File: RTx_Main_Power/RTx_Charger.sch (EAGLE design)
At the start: 15 parts, among them IC1 TL331

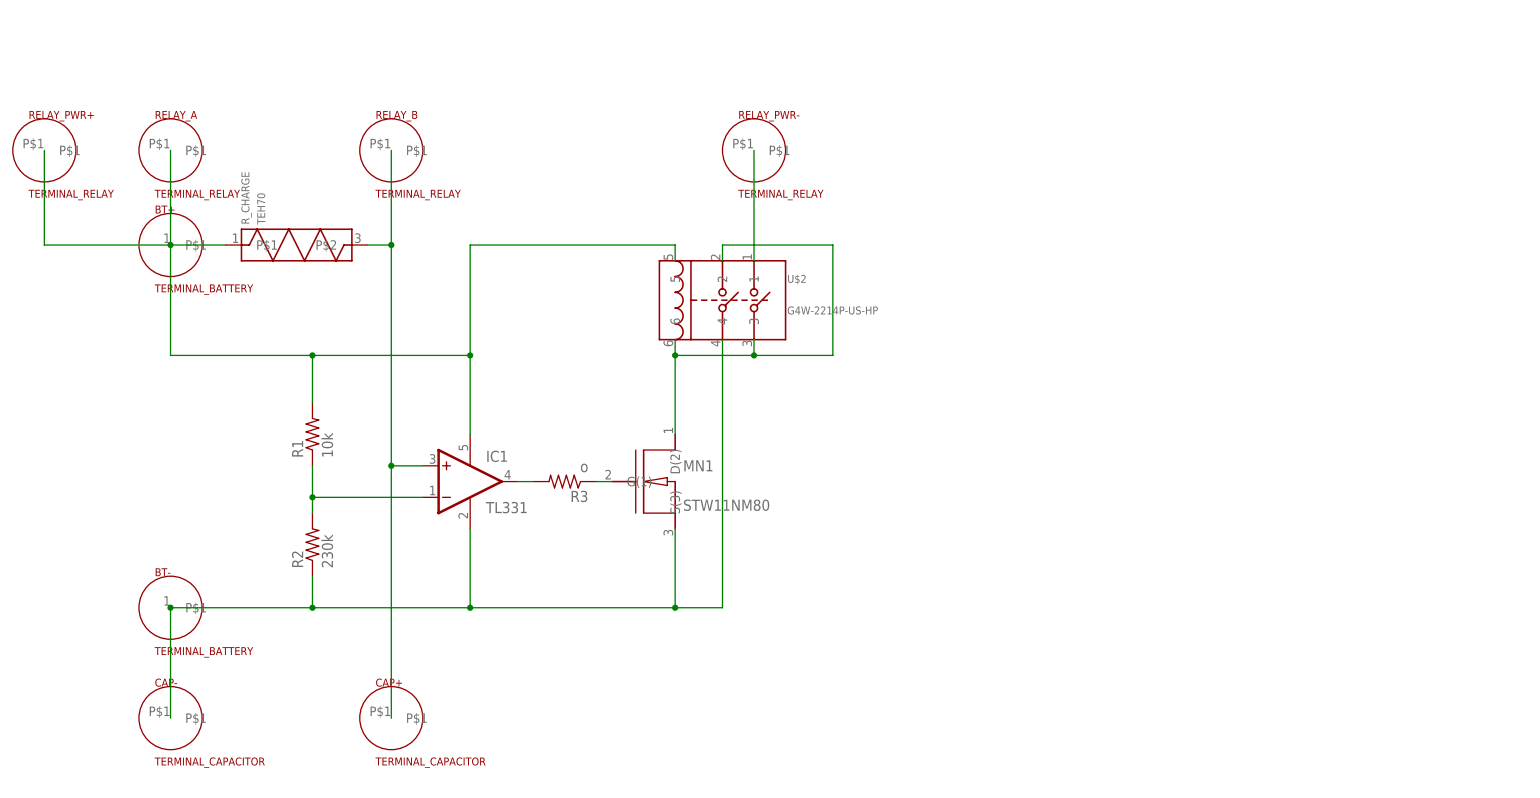
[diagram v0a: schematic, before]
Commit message: Most recent WPR.docx. Updated charger circuit to reflect potential issue fix.
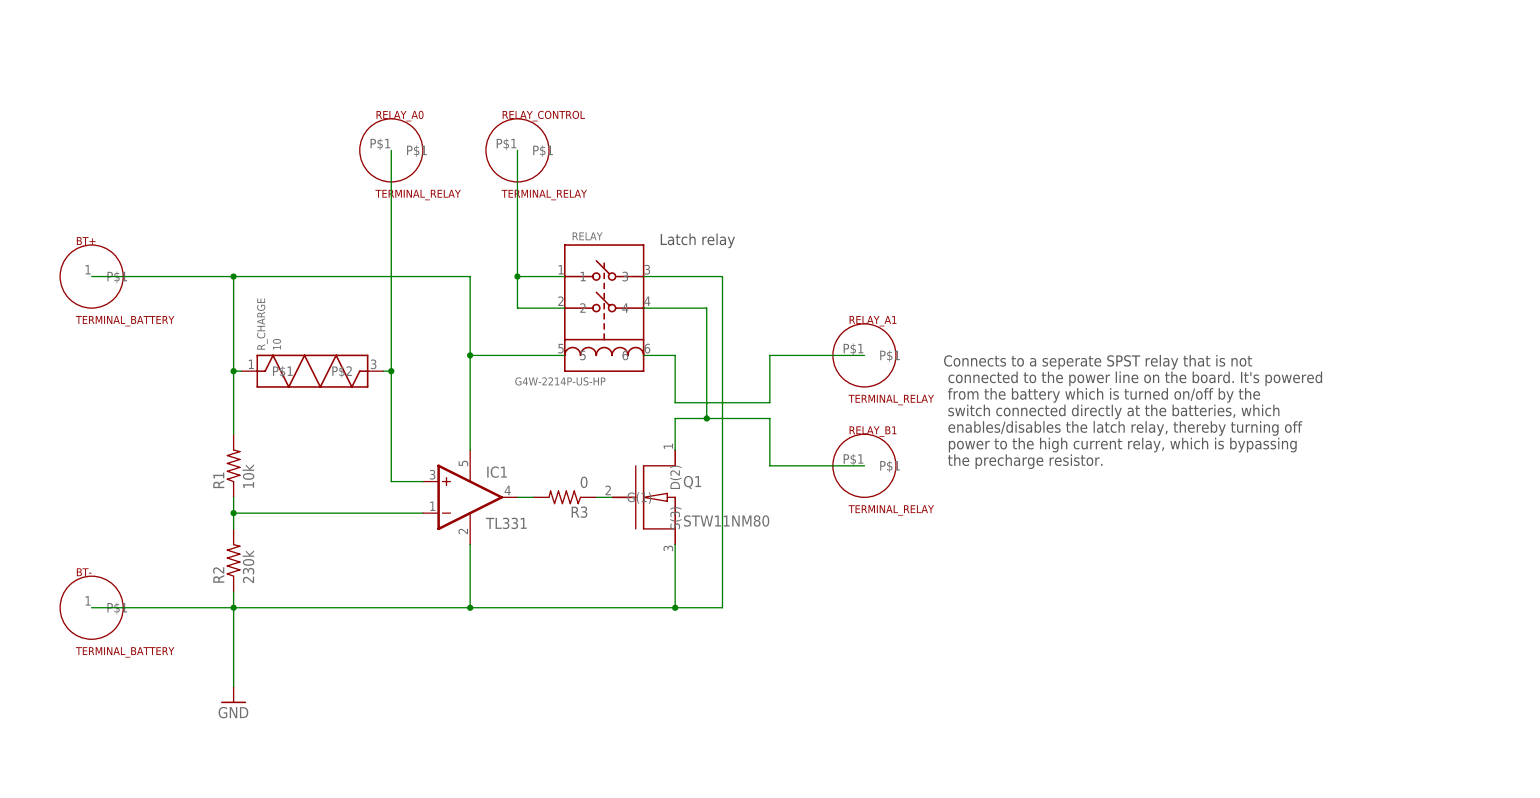
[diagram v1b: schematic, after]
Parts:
- removed CAP+, CAP-: TERMINAL_CAPACITOR, temp_library:TERMINAL_CAPACITOR
- removed MN1: STW11NM80, temp_library:STW11NM80
- removed RELAY_A, RELAY_PWR+, RELAY_PWR-: TERMINAL_RELAY, temp_library:TERMINAL_RELAY
- removed U$2: G4W-2214P-US-HP, temp_library:G4W-2214P-US-HP
- added Q1: STW11NM80, temp_library:STW11NM80
- added RELAY: G4W-2214P-US-HP, temp_library:G4W-2214P-US-HP
- added RELAY_A1, RELAY_B1, RELAY_CONTROL: TERMINAL_RELAY, temp_library:TERMINAL_RELAY
- R3: value o -> 0
- R_CHARGE: value TEH70 -> 10
- renumbered RELAY_B to RELAY_A0
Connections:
- removed net N$2: RELAY_PWR-.P$1, U$2.1
- new net N$7: RELAY.1, RELAY.2, RELAY_CONTROL.P$1
- new net N$8: RELAY.6, RELAY_A1.P$1
- new net N$9: Q1.D(2), RELAY.4, RELAY_B1.P$1
- net GND: now also Q1.S(3), RELAY.3; no longer CAP-.P$1, MN1.S(3), U$2.4
- net N$3: now also BT+.P$1; no longer MN1.D(2), U$2.2, U$2.3, U$2.6
- net N$5: now also Q1.G(1); no longer MN1.G(1)
- net N$6: no longer CAP+.P$1
- net VDD: now also RELAY.5; no longer BT+.P$1, RELAY_A.P$1, RELAY_PWR+.P$1, U$2.5
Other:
- note added: "Connects to a seperate SPST relay that is not connected to the power line on the board. It's powered from the battery which is turned on/off by the switch connected directly at the batteries, which enables/disables the latch relay, thereby turning off power to the high current relay, which is bypassing the precharge resistor."
- note added: "Latch relay"
- moved on the sheet: BT+, BT-, IC1, R1, R2, R3, R_CHARGE

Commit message: Added additional terminals to RTx_Charger board.
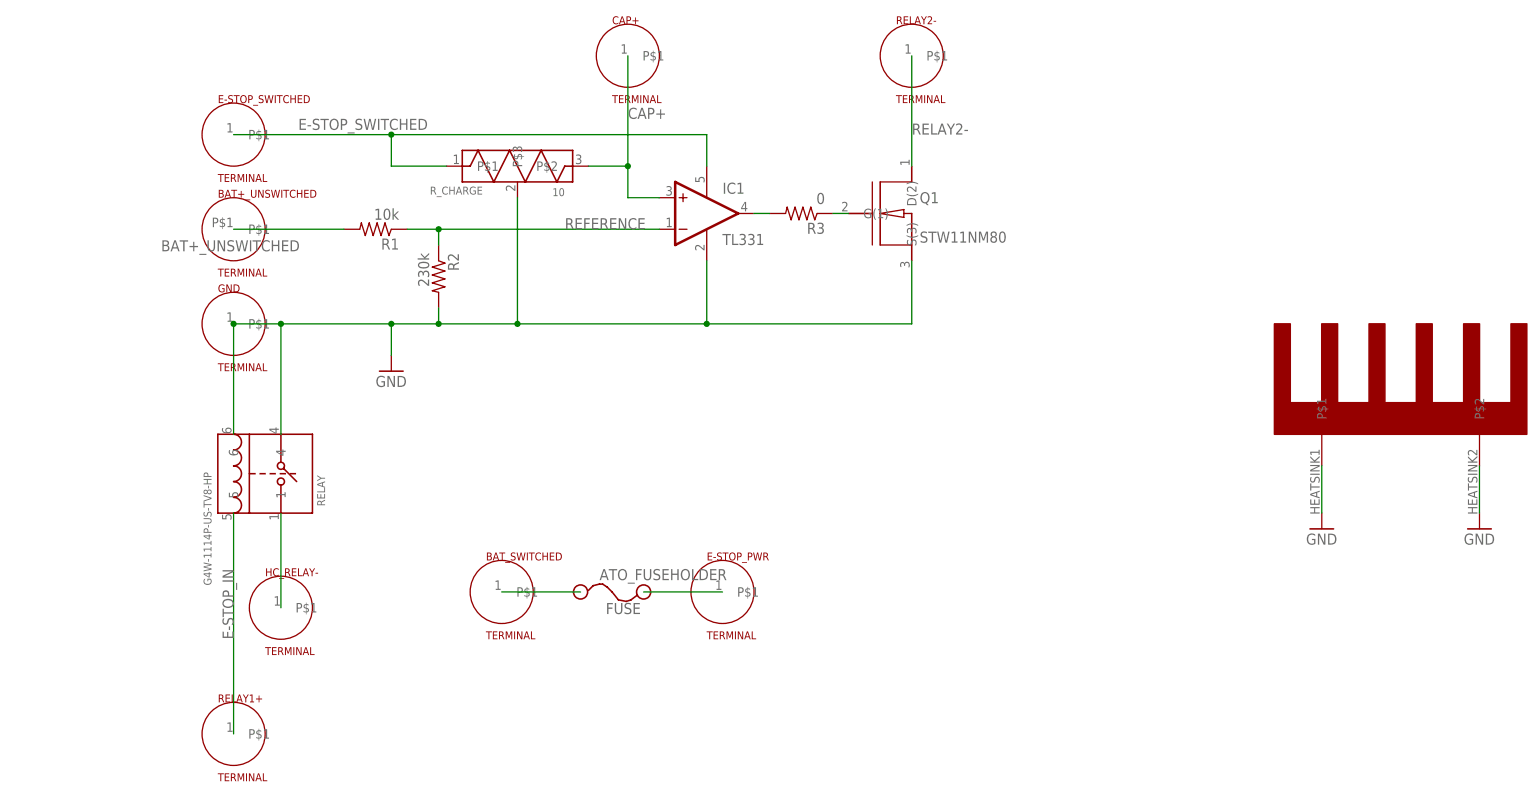
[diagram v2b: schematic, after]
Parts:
- removed BT+, BT-: TERMINAL_BATTERY, temp_library:TERMINAL_BATTERY
- removed RELAY_A0, RELAY_A1, RELAY_B1, RELAY_CONTROL: TERMINAL_RELAY, temp_library:TERMINAL_RELAY
- added BAT+_UNSWITCHED: TERMINAL, temp_library:TERMINAL_RELAY
- added BAT_SWITCHED, CAP+, E-STOP_PWR, E-STOP_SWITCHED, GND, HC_RELAY-, RELAY1+, RELAY2-: TERMINAL, temp_library:TERMINAL_BATTERY
- added FUSE: ATO_FUSEHOLDER, temp_library:FUSEATO_FUSEHOLDER
- added HEATSINK: WA-T247-101E, temp_library:WA-T247-101E
- RELAY: value G4W-2214P-US-HP -> G4W-1114P-US-TV8-HP; device temp_library:G4W-2214P-US-HP -> temp_library:G4W-1114P-US-TV8-HP
- R_CHARGE: device motorFeedback:TEH70 -> temp_library:TEH70
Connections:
- removed net N$3: BT+.P$1
- removed net N$4: IC1.-IN, R1.1, R2.2
- removed net N$6: IC1.+IN, RELAY_A0.P$1, R_CHARGE.P$2
- removed net N$7: RELAY.1, RELAY.2, RELAY_CONTROL.P$1
- removed net N$8: RELAY.6, RELAY_A1.P$1
- removed net N$9: Q1.D(2), RELAY.4, RELAY_B1.P$1
- removed net VDD: IC1.V+, R1.2, RELAY.5, R_CHARGE.P$1
- new net BAT+_UNSWITCHED: BAT+_UNSWITCHED.P$1, R1.2
- new net BAT_SWITCHED: BAT_SWITCHED.P$1, FUSE.C
- new net CAP+: CAP+.P$1, IC1.+IN, R_CHARGE.P$2
- new net E-STOP_IN: RELAY.5, RELAY1+.P$1
- new net E-STOP_PWR: E-STOP_PWR.P$1, FUSE.A
- new net E-STOP_SWITCHED: E-STOP_SWITCHED.P$1, IC1.V+, R_CHARGE.P$1
- new net HC_RELAY-: HC_RELAY-.P$1, RELAY.1
- new net REFERENCE: IC1.-IN, R1.1, R2.1
- new net RELAY2-: Q1.D(2), RELAY2-.P$1
- net GND: now also GND.P$1, HEATSINK.P$1, HEATSINK.P$2, R2.2, RELAY.4, RELAY.6, R_CHARGE.P$3; no longer BT-.P$1, R2.1, RELAY.3
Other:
- note removed: "Connects to a seperate SPST relay that is not connected to the power line on the board. It's powered from the battery which is turned on/off by the switch connected directly at the batteries, which enables/disables the latch relay, thereby turning off power to the high current relay, which is bypassing the precharge resistor."
- note removed: "Latch relay"
- moved on the sheet: IC1, Q1, R1, R2, R3

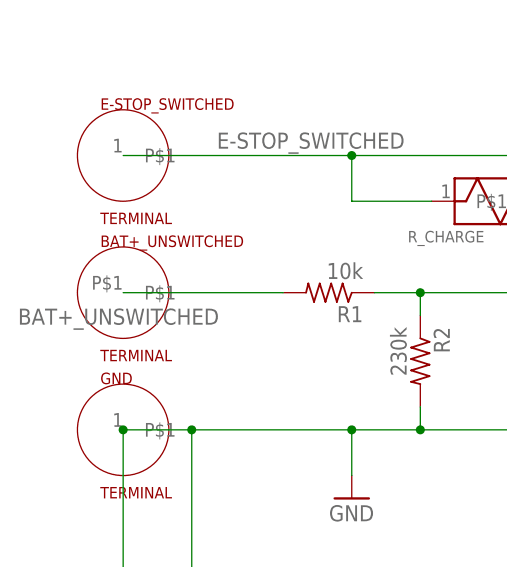
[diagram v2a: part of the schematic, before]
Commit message: RTx_Charger board layout changed.
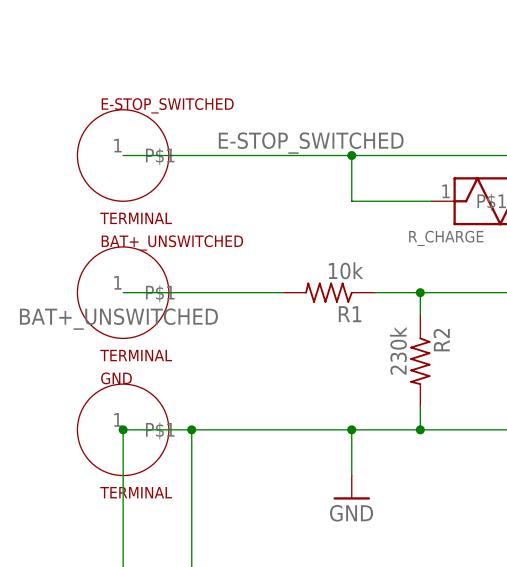
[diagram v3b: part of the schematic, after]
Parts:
- BAT+_UNSWITCHED: device temp_library:TERMINAL_RELAY -> temp_library:TERMINALSTUD
- BAT_SWITCHED, E-STOP_SWITCHED, HC_RELAY-, RELAY1+, RELAY2-: device temp_library:TERMINAL_BATTERY -> temp_library:TERMINALNO_STUD
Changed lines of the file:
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@@
 <part name="GND1" library="motorFeedback" deviceset="GND" device=""/>
 <part name="R_CHARGE" library="temp_library" deviceset="TEH70" device="" value="10"/>
-<part name="BAT+_UNSWITCHED" library="temp_library" deviceset="TERMINAL_RELAY" device="" value="TERMINAL"/>
+<part name="BAT+_UNSWITCHED" library="temp_library" deviceset="TERMINAL" device="STUD" value="TERMINAL"/>
 <part name="GND" library="temp_library" deviceset="TERMINAL_BATTERY" device="" value="TERMINAL"/>
-<part name="E-STOP_SWITCHED" library="temp_library" deviceset="TERMINAL_BATTERY" device="" value="TERMINAL"/>
-<part name="RELAY2-" library="temp_library" deviceset="TERMINAL_BATTERY" device="" value="TERMINAL"/>
+<part name="E-STOP_SWITCHED" library="temp_library" deviceset="TERMINAL" device="NO_STUD" value="TERMINAL"/>
+<part name="RELAY2-" library="temp_library" deviceset="TERMINAL" device="NO_STUD" value="TERMINAL"/>
 <part name="CAP+" library="temp_library" deviceset="TERMINAL_BATTERY" device="" value="TERMINAL"/>
 <part name="R1" library="motorFeedback" deviceset="R-US_" device="R1206" value="10k"/>
@@
 <part name="GND3" library="motorFeedback" deviceset="GND" device=""/>
 <part name="FUSE" library="temp_library" deviceset="FUSE" device="ATO_FUSEHOLDER" value="ATO_FUSEHOLDER"/>
-<part name="BAT_SWITCHED" library="temp_library" deviceset="TERMINAL_BATTERY" device="" value="TERMINAL"/>
+<part name="BAT_SWITCHED" library="temp_library" deviceset="TERMINAL" device="NO_STUD" value="TERMINAL"/>
 <part name="E-STOP_PWR" library="temp_library" deviceset="TERMINAL_BATTERY" device="" value="TERMINAL"/>
-<part name="RELAY1+" library="temp_library" deviceset="TERMINAL_BATTERY" device="" value="TERMINAL"/>
-<part name="HC_RELAY-" library="temp_library" deviceset="TERMINAL_BATTERY" device="" value="TERMINAL"/>
+<part name="RELAY1+" library="temp_library" deviceset="TERMINAL" device="NO_STUD" value="TERMINAL"/>
+<part name="HC_RELAY-" library="temp_library" deviceset="TERMINAL" device="NO_STUD" value="TERMINAL"/>
 <part name="RELAY" library="temp_library" deviceset="G4W-1114P-US-TV8-HP" device=""/>
 </parts>

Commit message: Completed charger board and BOM.
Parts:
- CAP+, E-STOP_PWR, GND: device temp_library:TERMINAL_BATTERY -> temp_library:TERMINALSTUD
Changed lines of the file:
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@@
 <part name="R_CHARGE" library="temp_library" deviceset="TEH70" device="" value="10"/>
 <part name="BAT+_UNSWITCHED" library="temp_library" deviceset="TERMINAL" device="STUD" value="TERMINAL"/>
-<part name="GND" library="temp_library" deviceset="TERMINAL_BATTERY" device="" value="TERMINAL"/>
+<part name="GND" library="temp_library" deviceset="TERMINAL" device="STUD" value="TERMINAL"/>
 <part name="E-STOP_SWITCHED" library="temp_library" deviceset="TERMINAL" device="NO_STUD" value="TERMINAL"/>
 <part name="RELAY2-" library="temp_library" deviceset="TERMINAL" device="NO_STUD" value="TERMINAL"/>
-<part name="CAP+" library="temp_library" deviceset="TERMINAL_BATTERY" device="" value="TERMINAL"/>
+<part name="CAP+" library="temp_library" deviceset="TERMINAL" device="STUD" value="TERMINAL"/>
 <part name="R1" library="motorFeedback" deviceset="R-US_" device="R1206" value="10k"/>
 <part name="R2" library="motorFeedback" deviceset="R-US_" device="R1206" value="230k"/>
@@
 <part name="FUSE" library="temp_library" deviceset="FUSE" device="ATO_FUSEHOLDER" value="ATO_FUSEHOLDER"/>
 <part name="BAT_SWITCHED" library="temp_library" deviceset="TERMINAL" device="NO_STUD" value="TERMINAL"/>
-<part name="E-STOP_PWR" library="temp_library" deviceset="TERMINAL_BATTERY" device="" value="TERMINAL"/>
+<part name="E-STOP_PWR" library="temp_library" deviceset="TERMINAL" device="STUD" value="TERMINAL"/>
 <part name="RELAY1+" library="temp_library" deviceset="TERMINAL" device="NO_STUD" value="TERMINAL"/>
 <part name="HC_RELAY-" library="temp_library" deviceset="TERMINAL" device="NO_STUD" value="TERMINAL"/>
